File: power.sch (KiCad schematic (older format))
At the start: 27 parts, among them J10 Conn_01x02, J11 Conn_01x02, J8 Conn_01x02, J9 Conn_01x02, Q3 DMN63D8LDW, SW3 SW_Push, U3 MCP16331T-E/CH, U4 BTS50080-1TEA, U5 DC_DC_POL

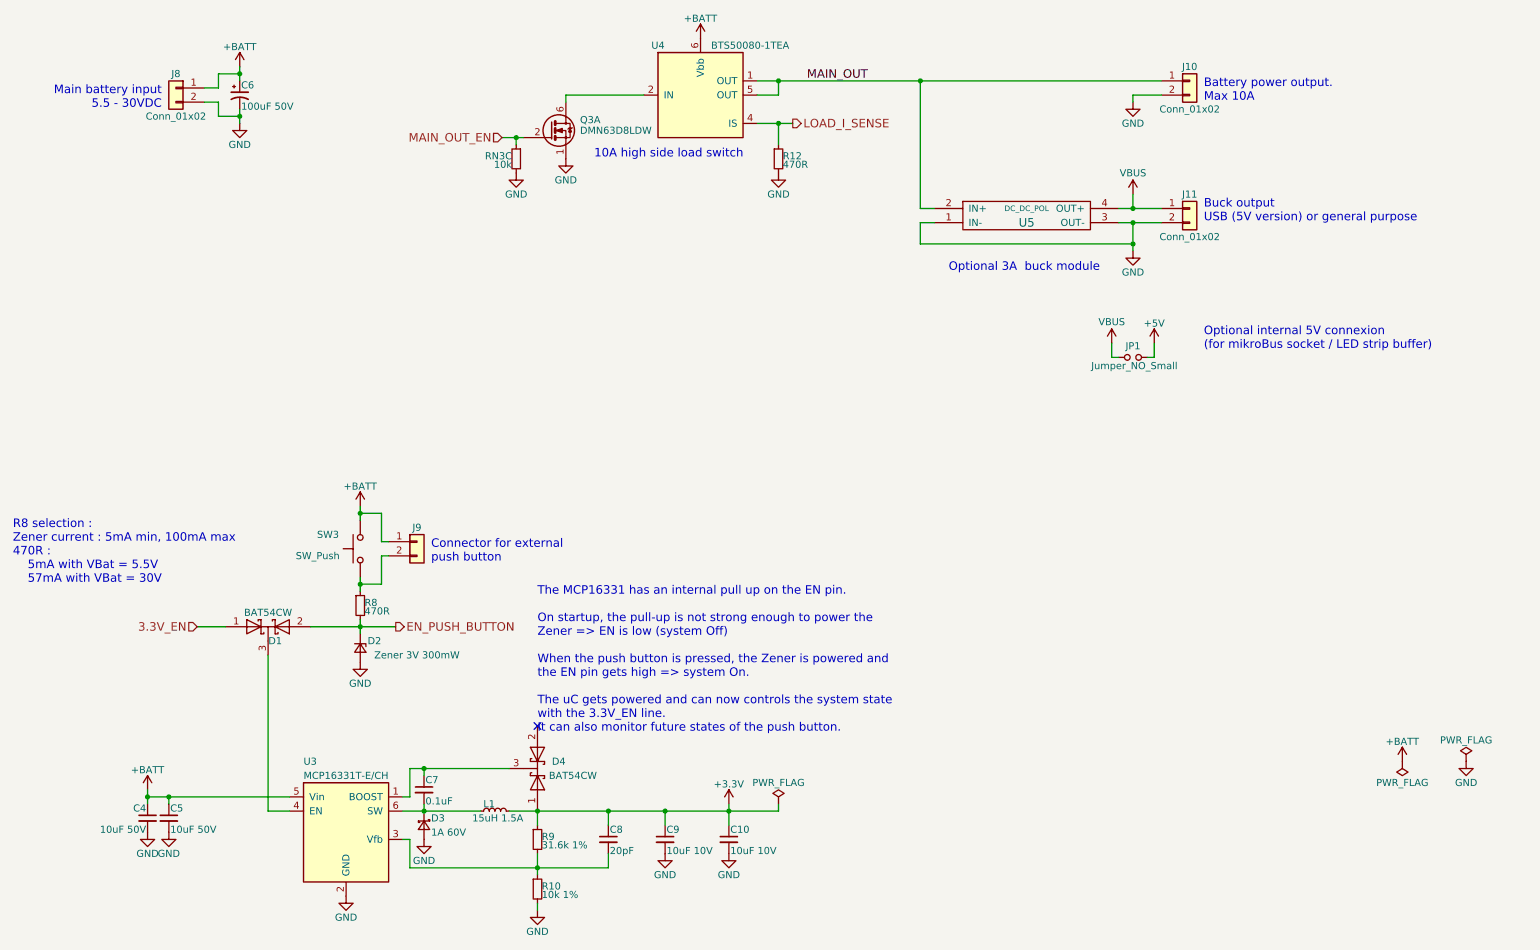
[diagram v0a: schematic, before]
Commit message: Component placement WIP - multiple Hammond enclosures drawn
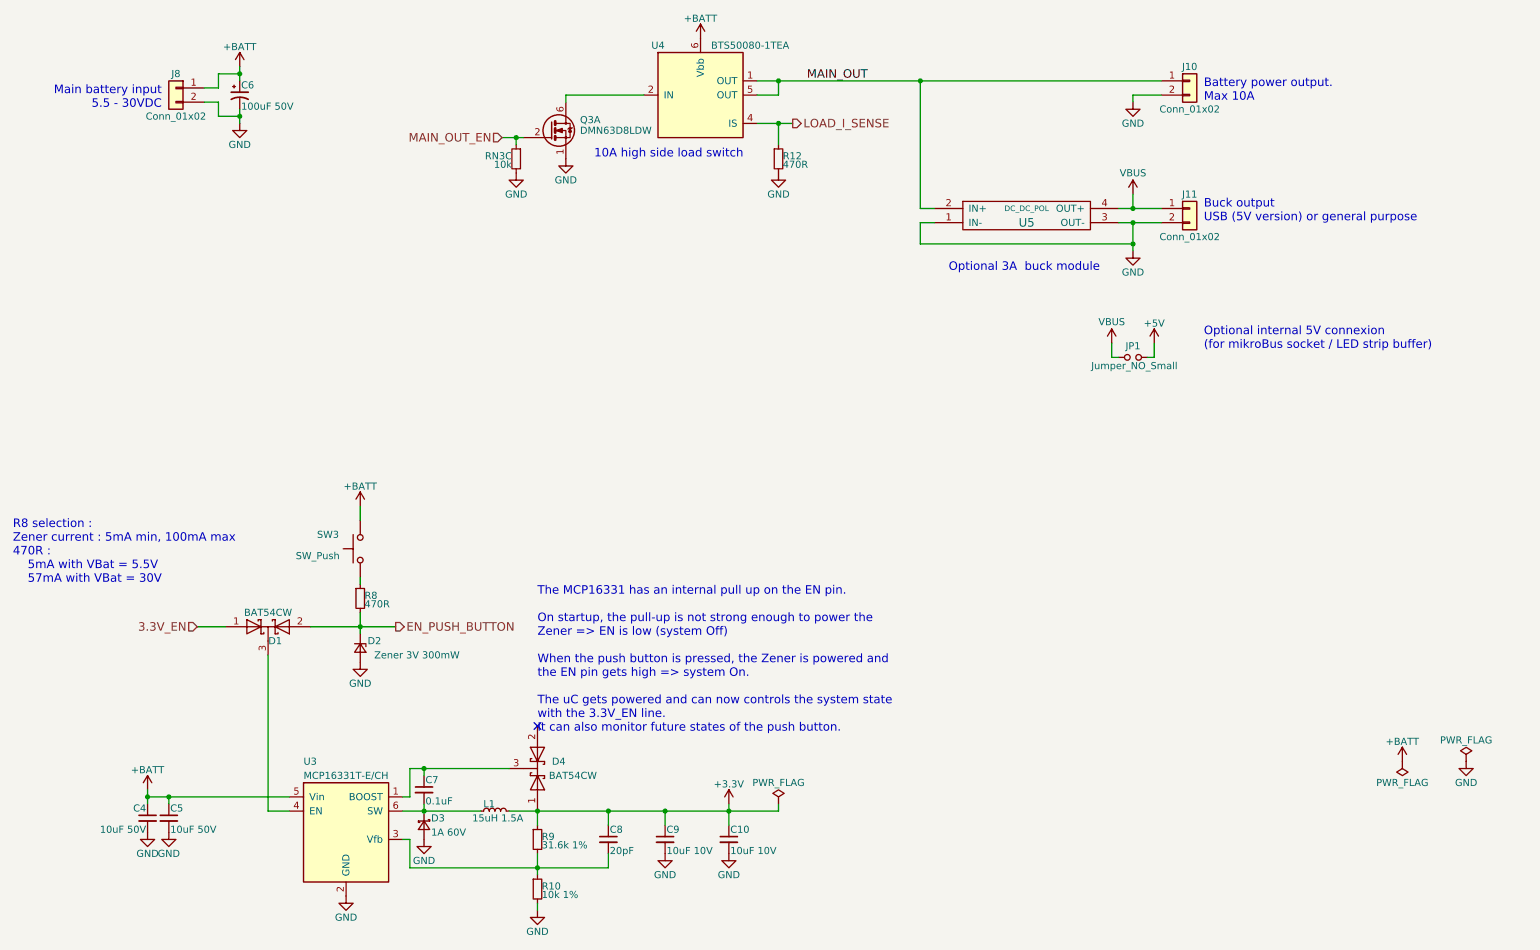
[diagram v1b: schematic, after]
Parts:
- removed J9: Conn_01x02, Connectors_TestPoints:Test_Point_2Pads_Pitch2.54mm_Drill0.8mm, symbol Conn_01x02
- RN3: footprint (none) -> Resistors_SMD:R_Array_Convex_4x0402
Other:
- note removed: "Connector for external\npush button"
- moved on the sheet: R8
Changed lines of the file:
@@
-$EndComp
-$Comp
-L Conn_01x02 J9
-U 1 1 5A9FC7F6
-P 3400 4650
-F 0 "J9" H 3400 4750 50  0000 C CNN
-F 1 "Conn_01x02" H 3400 4450 50  0001 C CNN
-F 2 "Connectors_TestPoints:Test_Point_2Pads_Pitch2.54mm_Drill0.8mm" H 3400 4650 50  0001 C CNN
-F 3 "" H 3400 4650 50  0001 C CNN
-	1    3400 4650
-	1    0    0    -1
 $EndComp
 $Comp
@@
 	2000 1450 1900 1450
 Wire Wire Line
-	5800 1400 8650 1400
+	5800 1400 5950 1400
+Wire Wire Line
+	5950 1400 6950 1400
+Wire Wire Line
+	6950 1400 8650 1400
 Wire Wire Line
 	8650 1500 8450 1500
@@
 MAIN_OUT_EN
 Wire Wire Line
-	8350 2400 8650 2400
+	8350 2400 8450 2400
+Wire Wire Line
+	8450 2400 8650 2400
 Connection ~ 8450 2300
 Wire Wire Line
@@
 	6950 2550 8450 2550
 Wire Wire Line
-	8450 2400 8450 2600
+	8450 2400 8450 2550
+Wire Wire Line
+	8450 2550 8450 2600
 Connection ~ 8450 2400
 $Comp
@@
 $EndComp
 Wire Wire Line
-	1500 6400 1500 6500
-Wire Wire Line
-	1500 6450 2500 6450
+	1500 6400 1500 6450
+Wire Wire Line
+	1500 6450 1500 6500
+Wire Wire Line
+	1500 6450 1650 6450
+Wire Wire Line
+	1650 6450 2500 6450
 Wire Wire Line
 	1650 6450 1650 6500
@@
 	3350 6750 3350 6950
 Wire Wire Line
-	3350 6950 4750 6950
+	3350 6950 4250 6950
+Wire Wire Line
+	4250 6950 4750 6950
 $Comp
 L GND #PWR038
@@
 $EndComp
 Wire Wire Line
-	3300 6550 3850 6550
+	3300 6550 3450 6550
+Wire Wire Line
+	3450 6550 3850 6550
 Wire Wire Line
 	3450 6550 3450 6500
@@
 	3350 6450 3350 6250
 Wire Wire Line
-	3350 6250 4050 6250
+	3350 6250 3450 6250
+Wire Wire Line
+	3450 6250 4050 6250
 Wire Wire Line
 	3450 6250 3450 6300
@@
 Connection ~ 3450 6250
 Wire Wire Line
-	4050 6550 5950 6550
+	4050 6550 4250 6550
+Wire Wire Line
+	4250 6550 4750 6550
+Wire Wire Line
+	4750 6550 5150 6550
+Wire Wire Line
+	5150 6550 5600 6550
+Wire Wire Line
+	5600 6550 5950 6550
 $Comp
 L R_Small R9
@@
 Connection ~ 4250 6550
 Wire Wire Line
-	4250 6850 4250 7000
+	4250 6850 4250 6950
+Wire Wire Line
+	4250 6950 4250 7000
 Connection ~ 4250 6950
 Wire Wire Line
@@
 Connection ~ 4750 6550
 Wire Wire Line
-	5600 6500 5600 6650
+	5600 6500 5600 6550
+Wire Wire Line
+	5600 6550 5600 6650
 Connection ~ 5150 6550
 $Comp
@@
 	3000 4400 3000 4500
 Wire Wire Line
-	3000 4450 3150 4450
-Wire Wire Line
-	3150 4450 3150 4650
-Wire Wire Line
-	3150 4650 3200 4650
-Connection ~ 3000 4450
-Wire Wire Line
-	3200 4750 3150 4750
-Wire Wire Line
-	3150 4750 3150 4950
-Wire Wire Line
-	3150 4950 3000 4950
-Wire Wire Line
-	3000 4900 3000 5000
-Text Notes 3500 4800 0    60   ~ 0
-Connector for external\npush button
+	3000 4900 3000 4950
 $Comp
 L R_Small R8
 U 1 1 5AA0358A
-P 3000 5100
-F 0 "R8" H 3030 5120 50  0000 L CNN
-F 1 "470R" H 3030 5060 50  0000 L CNN
-F 2 "Resistors_SMD:R_0603" H 3000 5100 50  0001 C CNN
-F 3 "" H 3000 5100 50  0001 C CNN
-	1    3000 5100
-	1    0    0    -1
-$EndComp
-Connection ~ 3000 4950
-Wire Wire Line
-	3000 5200 3000 5300
+P 3000 5050
+F 0 "R8" H 3030 5070 50  0000 L CNN
+F 1 "470R" H 3030 5010 50  0000 L CNN
+F 2 "Resistors_SMD:R_0603" H 3000 5050 50  0001 C CNN
+F 3 "" H 3000 5050 50  0001 C CNN
+	1    3000 5050
+	1    0    0    -1
+$EndComp
+Wire Wire Line
+	3000 5150 3000 5250
+Wire Wire Line
+	3000 5250 3000 5300
 $Comp
 L GND #PWR045
@@
 	1850 5250 2050 5250
 Wire Wire Line
-	2650 5250 3250 5250
+	2650 5250 3000 5250
+Wire Wire Line
+	3000 5250 3250 5250
 Connection ~ 3000 5250
 Wire Wire Line
@@
 	2000 1350 2150 1350
 Wire Wire Line
-	2150 1300 2150 1400
+	2150 1300 2150 1350
+Wire Wire Line
+	2150 1350 2150 1400
 Connection ~ 2150 1350
 Wire Wire Line
 	2000 1650 2150 1650
 Wire Wire Line
-	2150 1600 2150 1700
+	2150 1600 2150 1650
+Wire Wire Line
+	2150 1650 2150 1700
 Connection ~ 2150 1650
 Wire Wire Line
-	8350 2300 8650 2300
+	8350 2300 8450 2300
+Wire Wire Line
+	8450 2300 8650 2300
 $Comp
 L BTS50080-1TEA U4
@@
 $EndComp
 Wire Wire Line
-	4000 1800 4150 1800
+	4000 1800 4100 1800
+Wire Wire Line
+	4100 1800 4150 1800
 Wire Wire Line
 	4100 1800 4100 1850
@@
 $EndComp
 Wire Wire Line
-	5800 1700 6050 1700
+	5800 1700 5950 1700
+Wire Wire Line
+	5950 1700 6050 1700
 Wire Wire Line
 	5950 1700 5950 1850
@@
 F 0 "RN3" H 4130 1970 50  0000 L CNN
 F 1 "10k" H 4130 1910 50  0000 L CNN
-F 2 "" H 4100 1950 50  0001 C CNN
+F 2 "Resistors_SMD:R_Array_Convex_4x0402" H 4100 1950 50  0001 C CNN
 F 3 "" H 4100 1950 50  0001 C CNN
 	3    4100 1950

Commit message: Almost all components placed... Saving before mirroring everything
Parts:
- removed J11: Conn_01x02, Connectors_Terminal_Blocks:TerminalBlock_Pheonix_PT-3.5mm_2pol, symbol Conn_01x02
- D3: footprint Diodes_SMD:D_SMA -> Diodes_SMD:D_SOD-123F
- SW3: footprint Buttons_Switches_THT:SW_Tactile_SPST_Angled_PTS645Vx58-2LFS -> tom_kicad_lib:SW_Tactile_SPST_Angled_PTS645Vx58-2LFS_horiz_pads
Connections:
- net MAIN_OUT renamed +VSW
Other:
- note added: "Optional internal 5V connexion \n(for mikroBus socket)"
- note removed: "Buck output\nUSB (5V version) or general purpose"
- note removed: "Optional internal 5V connexion \n(for mikroBus socket / LED strip buffer)"

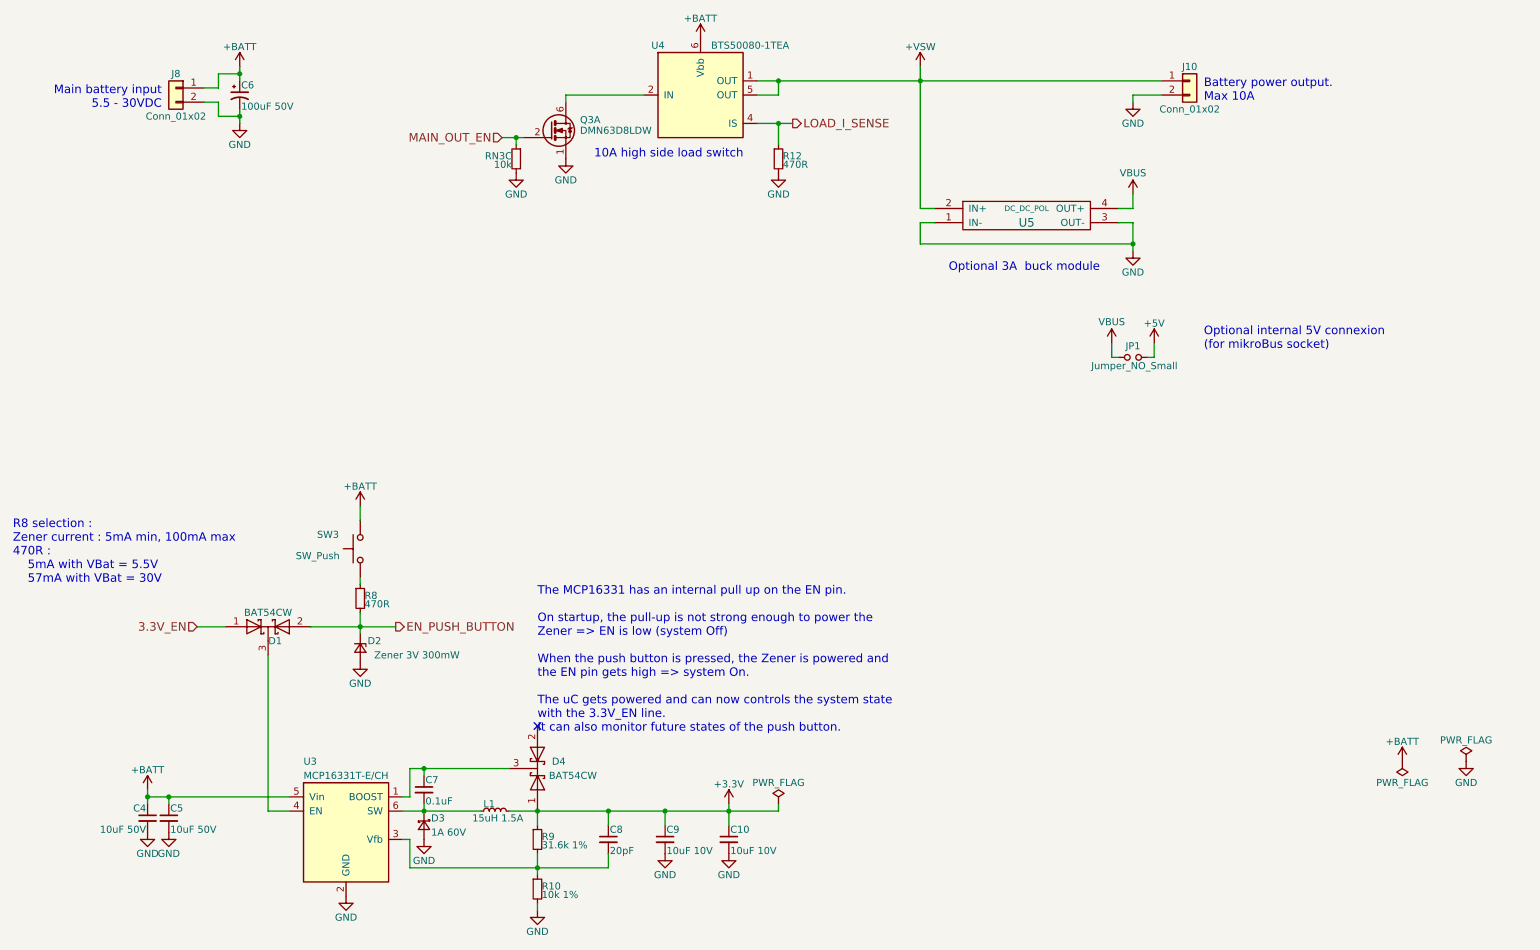
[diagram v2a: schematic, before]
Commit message: v1.0   Add 3D files with Hammond enclosures  fabrication outputs
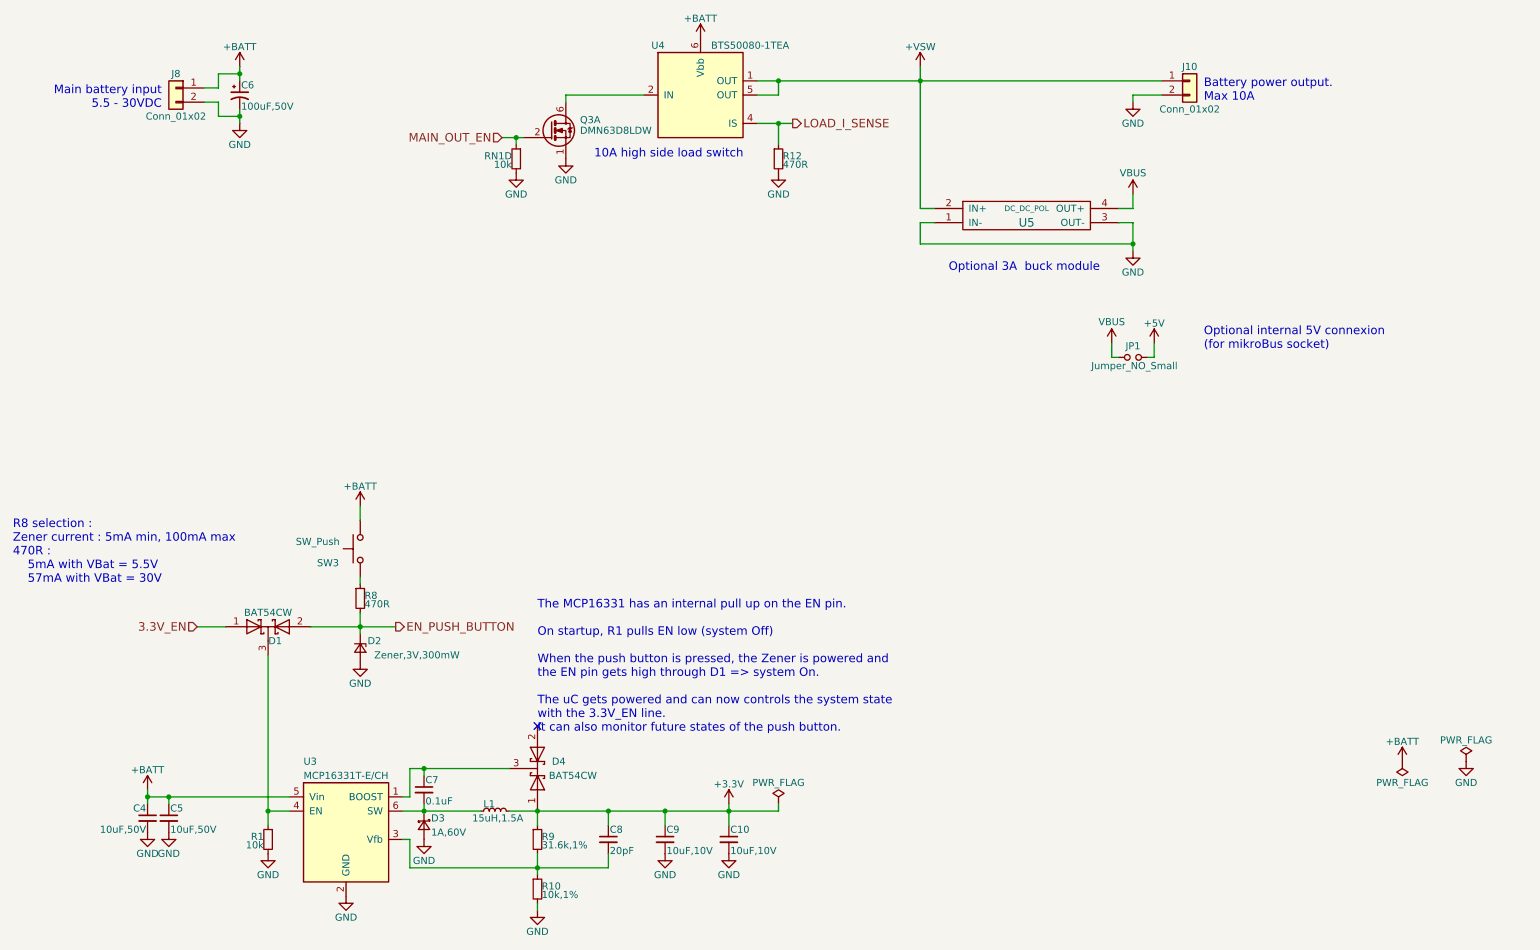
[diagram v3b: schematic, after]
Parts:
- added R1: 10k, Resistors_SMD:R_0603, symbol R_Small
- C10, C9: value 10uF 10V -> 10uF,10V
- C4, C5: value 10uF 50V -> 10uF,50V
- C6: value 100uF 50V -> 100uF,50V
- D2: value Zener 3V 300mW -> Zener,3V,300mW
- D3: value 1A 60V -> 1A,60V
- L1: value 15uH 1.5A -> 15uH,1.5A
- R10: value 10k 1% -> 10k,1%
- R9: value 31.6k 1% -> 31.6k,1%
- renumbered RN3 to RN1
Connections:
- net +BATT: now also SW3.2; no longer SW3.1
- net GND: now also RN1.5, R1.2; no longer RN1.6
- net MAIN_OUT_EN: now also RN1.4; no longer RN1.3
- net at D1.3 (K), U3.4 (EN): now also R1.1
- net at R8.1: now also SW3.1; no longer SW3.2
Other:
- note added: "The MCP16331 has an internal pull up on the EN pin.\n\nOn startup, R1 pulls EN low (system Off)\n\nWhen the push button is pressed, the Zener is powered and \nthe EN pin gets high through D1 => system On.\n\nThe uC gets powered and can now controls the system state \nwith the 3.3V_EN line.\nIt can also monitor future states of the push button."
- note removed: "The MCP16331 has an internal pull up on the EN pin.\n\nOn startup, the pull-up is not strong enough to power the\nZener => EN is low (system Off)\n\nWhen the push button is pressed, the Zener is powered and \nthe EN pin gets high => system On.\n\nThe uC gets powered and can now controls the system state \nwith the 3.3V_EN line.\nIt can also monitor future states of the push button."

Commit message: Update BOM & fab files
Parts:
- R1: value 10k -> 10k,1%
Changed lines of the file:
@@
 P 2350 6750
 F 0 "R1" H 2380 6770 50  0000 L CNN
-F 1 "10k" H 2380 6710 50  0000 L CNN
+F 1 "10k,1%" H 2380 6710 50  0000 L CNN
 F 2 "Resistors_SMD:R_0603" H 2350 6750 50  0001 C CNN
 F 3 "" H 2350 6750 50  0001 C CNN
